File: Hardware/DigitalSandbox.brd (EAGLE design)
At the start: 105.4 x 76.2 mm, 80 parts, among them J1 AVR_SPI_PRG_6NS, Q1 MOSFET-N, Q2 MOSFET-P, U1 MCP73831, U2 ATMEGA328, U3 C2031N-1A2-B10K-GP, U4 MCP9700, U5 FT232RLSSOP, U6 LIGHTSENSORALS, U7 V_REG_LDOSMD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

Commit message: Added Sparkle Values.
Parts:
- C1, C10, C11, C12, C13, C14, C6, C7, C8: device SparkFun:0603-CAP -> SparkFun-Capacitors:0603-CAP
- C2, C5: device SparkFun-Passives:0603-CAP -> SparkFun-Capacitors:0603-CAP
- C3: device SparkFun:EIA3528 -> SparkFun-Capacitors:EIA3528
- C9: device SparkFun:EIA3216 -> SparkFun-Capacitors:EIA3216
- D1, LED6, LED7: device SparkFun:LED-0603 -> SparkFun-LED:LED-0603
- R1, R13, R14, R15, R19, R2, R21, R22, R23, R24, R25, R26, R27, R3, R4, R5, R6, R7: device SparkFun-Passives:0603-RES -> SparkFun-Resistors:0603-RES
- R10, R11, R12, R8, R9: value 330 -> 300; device SparkFun-Resistors:0603 -> SparkFun-Resistors:0603-RES
- R17: value 200 -> 300; device SparkFun-Passives:0603-RES -> SparkFun-Resistors:0603-RES
- S1: device SparkFun:TACTILE_SWITCH_SMD -> SparkFun-Electromechanical:TACTILE_SWITCH_SMD
- S2: value AYZ0202 -> (none); device SparkFun:AYZ0202 -> SparkFun-Electromechanical:AYZ0202
- S3: device SparkFun:AYZ0202 -> SparkFun-Electromechanical:AYZ0202
- U1: device SparkFun:SOT23-5 -> SparkFun-PowerIC:SOT23-5
- U2: device SparkFun:TQFP32-08 -> SparkFun-DigitalIC:TQFP32-08
- U5: device SparkFun:SSOP28DB -> SparkFun-DigitalIC:SSOP28DB
- U8: value LMV358 -> LMV358SOIC; device SparkFun:SO08 -> SparkFun-AnalogIC:SO08
- U9: device SparkFun:MIC-9.7MM -> SparkFun-Sensors:MIC-9.7MM
- X1: value USB-SMD-NS -> USBSMD; device SparkFun:USB-MINIB-NOSTOP -> SparkFun-Connectors:USB-MINIB
- Y1: device SparkFun:RESONATOR-SMD -> SparkFun-FreqCtrl:RESONATOR-SMD
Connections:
- net GND: now also S1.2; no longer S1.3
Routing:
- net VBATT: track 21.9 -> 29.7 mm
- net GND: track 5.65 -> 0.00 mm
- net N$15: track 13.8 -> 8.17 mm

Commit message: updated Sparkle ID's
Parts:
- C4: device SparkFun:0603-CAP -> SparkFun-Capacitors:0603-CAP
- JP1: device SparkFun:JST-2-SMD -> SparkFun-Connectors:JST-2-SMD
- U$5: value LED-TRICOLOR-SMDPLCC-6-SMD -> LED-TRICOLOR; device Testing:PLCC-6-LED -> SparkFun-LED:PLCC-6-LED
- U3: value C2031N-1A2-B10K-GP -> 10K_LINEAR_SLIDE_POT_SMALL; device C2031N-1A2-B10K-GP:C2031N-1A2-B10K-GP -> SparkFun-Resistors:C2031N-1A2-B10K-GP
- U4: device SparkFun:SOT23-3 -> SparkFun-Sensors:SOT23-3
- U7: value V_REG_LDOSMD -> V_REG_MIC52053.3V
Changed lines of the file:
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@@
 <layer number="54" name="bGND_GNDA" color="1" fill="9" visible="no" active="no"/>
 <layer number="56" name="wert" color="7" fill="1" visible="yes" active="yes"/>
+<layer number="57" name="tCAD" color="7" fill="1" visible="no" active="no"/>
 <layer number="91" name="Nets" color="2" fill="1" visible="no" active="no"/>
 <layer number="92" name="Busses" color="1" fill="1" visible="no" active="no"/>
@@
 <layer number="97" name="Info" color="7" fill="1" visible="no" active="no"/>
 <layer number="98" name="Guide" color="6" fill="1" visible="no" active="no"/>
+<layer number="99" name="SpiceOrder" color="7" fill="1" visible="no" active="no"/>
 <layer number="100" name="Muster" color="7" fill="1" visible="no" active="no"/>
 <layer number="101" name="Patch_Top" color="12" fill="4" visible="yes" active="yes"/>
@@
 <layer number="132" name="bAdjust" color="7" fill="1" visible="yes" active="yes"/>
 <layer number="144" name="Drill_legend" color="7" fill="1" visible="yes" active="yes"/>
+<layer number="150" name="Notes" color="7" fill="1" visible="yes" active="yes"/>
 <layer number="151" name="_tDocu" color="7" fill="1" visible="yes" active="yes"/>
 <layer number="152" name="_bDocu" color="7" fill="1" visible="yes" active="yes"/>
+<layer number="153" name="FabDoc1" color="7" fill="1" visible="yes" active="yes"/>
+<layer number="154" name="FabDoc2" color="7" fill="1" visible="yes" active="yes"/>
+<layer number="155" name="FabDoc3" color="7" fill="1" visible="yes" active="yes"/>
 <layer number="199" name="Contour" color="7" fill="1" visible="yes" active="yes"/>
 <layer number="200" name="200bmp" color="1" fill="10" visible="no" active="no"/>
@@
 </autorouter>
 <elements>
-<element name="U4" library="SparkFun" package="SOT23-3" value="MCP9700" x="40.513" y="40.386" smashed="yes">
+<element name="U4" library="SparkFun-Sensors" package="SOT23-3" value="MCP9700" x="40.513" y="40.386" smashed="yes">
 <attribute name="NAME" x="39.6875" y="42.164" size="0.8128" layer="25" font="vector" ratio="15"/>
 <attribute name="VALUE" x="39.37" y="42.164" size="0.8128" layer="27" font="vector" ratio="15"/>
+<attribute name="PROD_ID" value="IC-08917" x="40.513" y="40.386" size="1.778" layer="27" display="off"/>
 </element>
 <element name="C8" library="SparkFun-Capacitors" package="0603-CAP" value="0.1uF" x="37.846" y="40.386" smashed="yes" rot="R90">
@@
 <attribute name="PROD_ID" value="XTAL-08895" x="15.113" y="42.926" size="1.778" layer="27" rot="R270" display="off"/>
 </element>
-<element name="JP1" library="SparkFun" package="JST-2-SMD" value="LiPo" x="10.668" y="72.517" smashed="yes">
+<element name="JP1" library="SparkFun-Connectors" package="JST-2-SMD" value="LiPo" x="10.668" y="72.517" smashed="yes">
 <attribute name="NAME" x="9.398" y="73.787" size="0.8128" layer="25" font="vector" ratio="15"/>
 <attribute name="VALUE" x="9.398" y="72.517" size="0.8128" layer="27" font="vector" ratio="15"/>
+<attribute name="PROD_ID" value="CONN-08352" x="10.668" y="72.517" size="1.778" layer="27" display="off"/>
 </element>
 <element name="S3" library="SparkFun-Electromechanical" package="AYZ0202" value="On/Off" x="10.033" y="54.991" smashed="yes" rot="R90">
@@
 <attribute name="PROD_ID" value="SWCH-08247" x="10.033" y="44.831" size="1.778" layer="27" rot="R270" display="off"/>
 </element>
-<element name="U3" library="C2031N-1A2-B10K-GP" package="C2031N-1A2-B10K-GP" value="C2031N-1A2-B10K-GP" x="50.673" y="9.017" smashed="yes">
+<element name="U3" library="SparkFun-Resistors" package="C2031N-1A2-B10K-GP" value="10K_LINEAR_SLIDE_POT_SMALL" x="50.673" y="9.017" smashed="yes">
 <attribute name="NAME" x="67.665" y="13.415" size="0.8128" layer="25" font="vector" ratio="15" rot="R180"/>
 <attribute name="VALUE" x="67.717" y="5.287" size="0.8128" layer="27" font="vector" ratio="15" rot="R180"/>
+<attribute name="PROD_ID" value="RES-11924" x="50.673" y="9.017" size="1.778" layer="27" display="off"/>
 </element>
 <element name="R17" library="SparkFun-Resistors" package="0603-RES" value="300" x="55.499" y="24.638" smashed="yes" rot="R90">
@@
 <attribute name="PROD_ID" value="CAP-00810" x="25.019" y="54.102" size="1.778" layer="27" rot="R270" display="off"/>
 </element>
-<element name="C4" library="SparkFun" package="0603-CAP" value="1.0uF" x="29.083" y="44.45" smashed="yes">
+<element name="C4" library="SparkFun-Capacitors" package="0603-CAP" value="1.0uF" x="29.083" y="44.45" smashed="yes">
 <attribute name="NAME" x="28.194" y="45.212" size="0.8128" layer="25" font="vector" ratio="15"/>
-<attribute name="VALUE" x="28.067" y="43.307" size="0.8128" layer="27" font="vector" ratio="15"/>
+<attribute name="VALUE" value="1.0uF" x="28.067" y="43.307" size="0.8128" layer="27" font="vector" ratio="15"/>
+<attribute name="PROD_ID" value="CAP-00868" x="29.083" y="44.45" size="1.778" layer="27" display="off"/>
 </element>
 <element name="R3" library="SparkFun-Resistors" package="0603-RES" value="10k" x="9.271" y="13.716" smashed="yes" rot="R180">
@@
 <attribute name="VALUE" x="38.227" y="68.58" size="1.27" layer="27"/>
 </element>
-<element name="U7" library="SparkFun-PowerIC" package="SOT23-5" value="V_REG_LDOSMD" x="31.75" y="68.072" smashed="yes" rot="R270">
+<element name="U7" library="SparkFun-PowerIC" package="SOT23-5" value="V_REG_MIC52053.3V" x="31.75" y="68.072" smashed="yes" rot="R270">
 <attribute name="NAME" x="33.909" y="68.961" size="0.8128" layer="25" font="vector" ratio="15" rot="R270"/>
-<attribute name="VALUE" x="31.5595" y="69.0245" size="0.8128" layer="27" font="vector" ratio="15" rot="R270"/>
+<attribute name="VALUE" value="3.3V/150mA" x="31.5595" y="69.0245" size="0.8128" layer="27" font="vector" ratio="15" rot="R270"/>
+<attribute name="PROD_ID" value="VREG-00822" x="31.75" y="68.072" size="1.778" layer="27" rot="R270" display="off"/>
 </element>
 <element name="C11" library="SparkFun-Capacitors" package="0603-CAP" value="0.1uF" x="35.687" y="69.723" smashed="yes" rot="R90">
@@
 <attribute name="PROD_ID" value="DIO-00809" x="28.448" y="37.084" size="1.778" layer="27" display="off"/>
 </element>
-<element name="U$5" library="Testing" package="PLCC-6-LED" value="LED-TRICOLOR-SMDPLCC-6-SMD" x="57.15" y="28.702"/>
+<element name="U$5" library="SparkFun-LED" package="PLCC-6-LED" value="LED-TRICOLOR" x="57.15" y="28.702">
+<attribute name="PROD_ID" value="DIO-12113" x="57.15" y="28.702" size="1.778" layer="27" display="off"/>
+</element>
 <element name="S5" library="SparkFun-Electromechanical" package="TACTILE_SWITCH_TALL" value="SWITCH-MOMENTARY-2SMD-4" x="83.185" y="24.13" rot="R180">
 <attribute name="PROD_ID" value="SWCH-11966" x="83.185" y="24.13" size="1.778" layer="27" rot="R180" display="off"/>
@@
 <contactref element="Y1" pad="2"/>
 <contactref element="U2" pad="21"/>
-<contactref element="JP1" pad="1"/>
 <contactref element="U1" pad="2"/>
 <contactref element="U4" pad="3"/>
@@
 <contactref element="S2" pad="1"/>
 <contactref element="S2" pad="4"/>
+<contactref element="JP1" pad="1"/>
 </signal>
 <signal name="VCC" class="1">
@@
 <signal name="VBATT">
 <contactref element="U1" pad="3"/>
-<contactref element="JP1" pad="2"/>
 <contactref element="C5" pad="1"/>
 <polygon width="0.254" layer="1" spacing="0.254" isolate="0.3048" rank="2">
@@
 <wire x1="5.715" y1="52.959" x2="5.715" y2="59.055" width="0.4064" layer="16"/>
 <wire x1="5.715" y1="59.055" x2="13.208" y2="66.548" width="0.4064" layer="16"/>
+<contactref element="JP1" pad="2"/>
 </signal>
 <signal name="N$33">

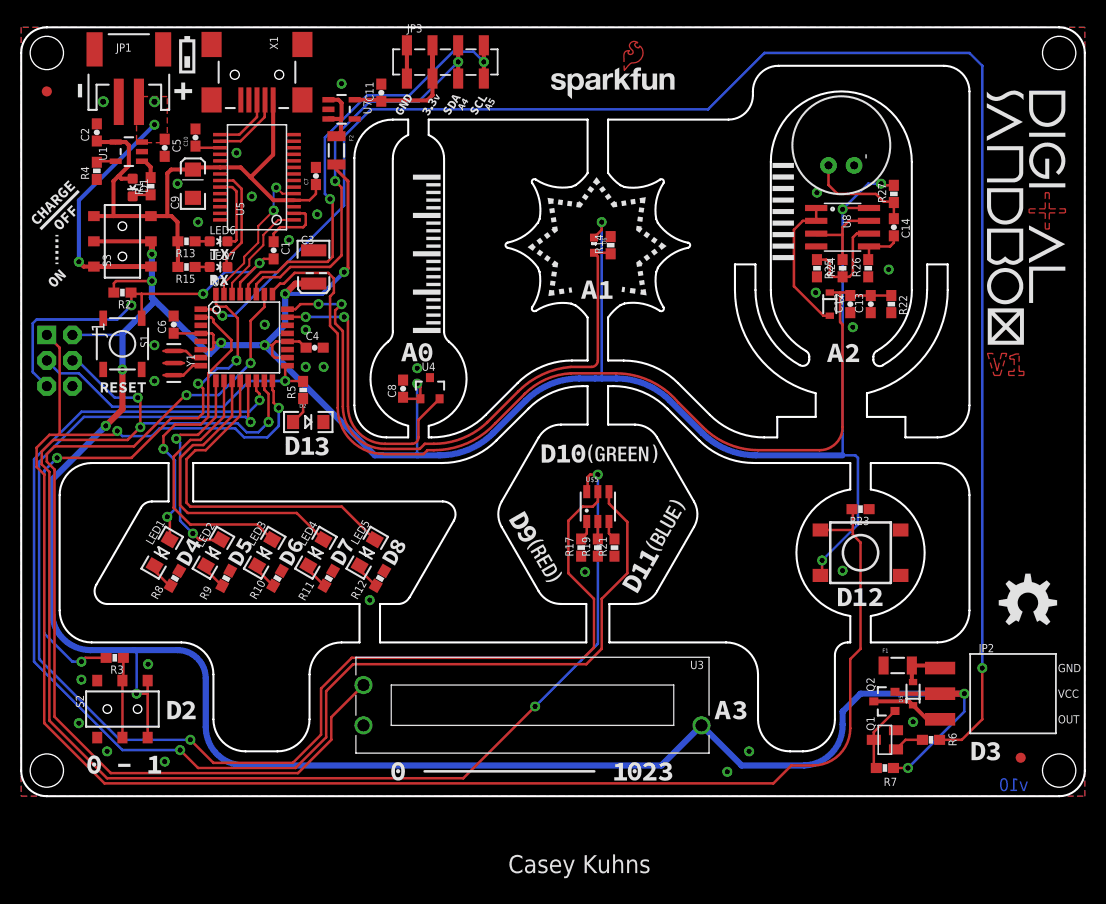
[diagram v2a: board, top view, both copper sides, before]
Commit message: fixed reset button orientation to work with standard push button
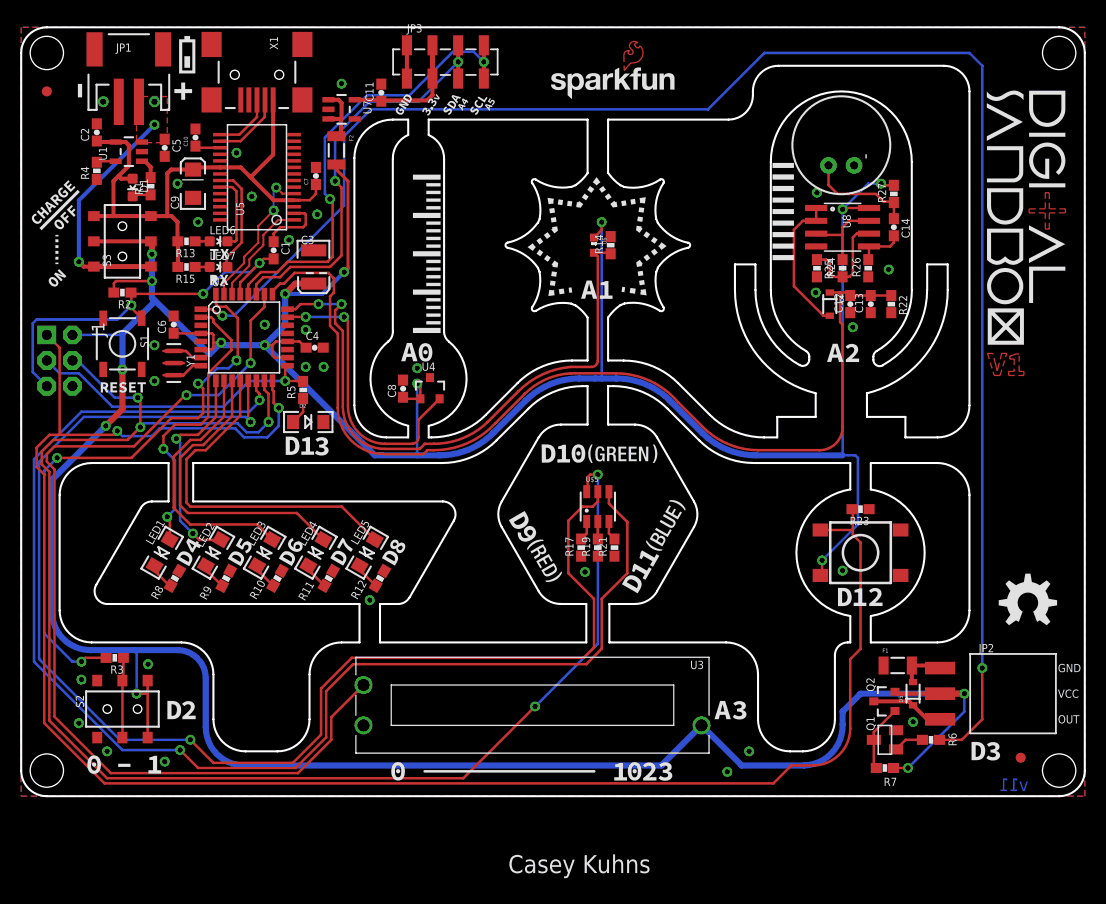
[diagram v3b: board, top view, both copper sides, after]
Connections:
- net GND: now also S1.3, S1.4; no longer S1.2
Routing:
- net RST: track 40.5 -> 39.8 mm
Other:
- board text added: "v11"
- board text removed: "v10"
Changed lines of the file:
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@@
 <wire x1="0" y1="2.54" x2="2.54" y2="0" width="0.2032" layer="20" curve="90"/>
 <text x="48.26" y="-7.62" size="1.778" layer="25">Casey Kuhns</text>
-<text x="99.822" y="0.508" size="1.27" layer="16" font="vector" ratio="20" rot="MR0">v10</text>
+<text x="99.822" y="0.508" size="1.27" layer="16" font="vector" ratio="20" rot="MR0">v11</text>
 <polygon width="0.001" layer="21">
 <vertex x="41.0694" y="68.9322"/>
@@
 <vertex x="105.41" y="0"/>
 </polygon>
-<contactref element="S1" pad="2"/>
 <contactref element="U8" pad="4"/>
 <contactref element="U9" pad="2"/>
@@
 <contactref element="S2" pad="4"/>
 <contactref element="JP1" pad="1"/>
+<contactref element="S1" pad="3"/>
+<contactref element="S1" pad="4"/>
 </signal>
 <signal name="VCC" class="1">
@@
 <contactref element="R2" pad="1"/>
 <contactref element="C1" pad="2"/>
-<contactref element="S1" pad="1"/>
 <wire x1="21.698" y1="49.7586" x2="21.698" y2="50.908" width="0.254" layer="1"/>
 <wire x1="21.698" y1="50.908" x2="23.622" y2="52.832" width="0.254" layer="1"/>
 <wire x1="23.622" y1="52.832" x2="24.042" y2="53.252" width="0.254" layer="1"/>
 <wire x1="25.019" y1="53.252" x2="24.042" y2="53.252" width="0.254" layer="1"/>
-<wire x1="11.938" y1="47.371" x2="11.938" y2="49.784" width="0.254" layer="1"/>
 <wire x1="10.883" y1="49.911" x2="11.01" y2="49.784" width="0.254" layer="1"/>
-<wire x1="11.01" y1="49.784" x2="11.938" y2="49.784" width="0.254" layer="1"/>
-<wire x1="11.938" y1="49.784" x2="18.034" y2="49.784" width="0.254" layer="1"/>
+<wire x1="11.01" y1="49.784" x2="18.034" y2="49.784" width="0.254" layer="1"/>
 <via x="18.034" y="49.784" extent="1-16" drill="0.508"/>
 <wire x1="18.034" y1="49.784" x2="20.193" y2="51.943" width="0.254" layer="16"/>
@@
 <wire x1="10.922" y1="48.641" x2="10.922" y2="49.872" width="0.254" layer="1"/>
 <wire x1="10.922" y1="49.872" x2="10.883" y2="49.911" width="0.254" layer="1"/>
+<contactref element="S1" pad="1"/>
+<wire x1="10.922" y1="48.641" x2="10.922" y2="48.387" width="0.254" layer="1"/>
+<wire x1="10.922" y1="48.387" x2="11.938" y2="47.371" width="0.254" layer="1"/>
 </signal>
 <signal name="D11">

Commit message: Chg to v12, thicken logo/art borders
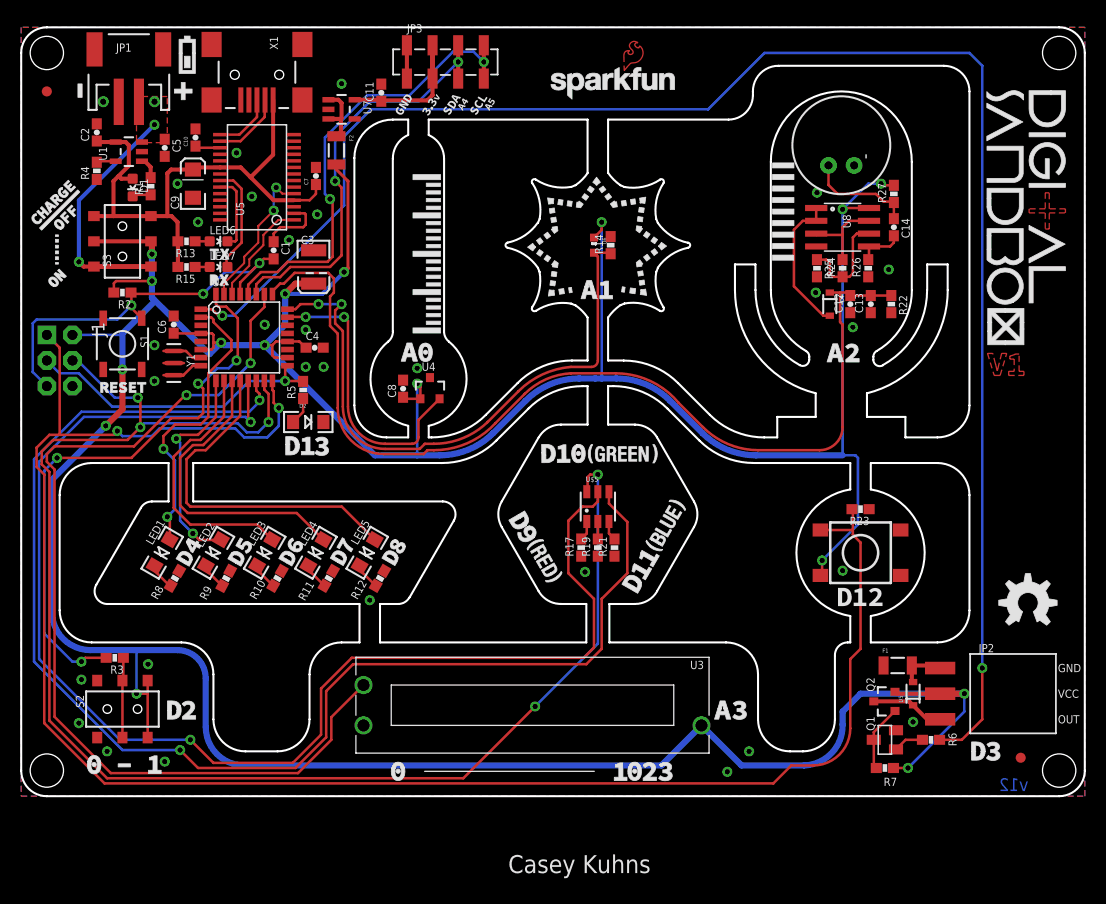
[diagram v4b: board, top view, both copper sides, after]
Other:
- board text added: "v12"
- board text removed: "v11"
